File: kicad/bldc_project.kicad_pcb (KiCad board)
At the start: 4 copper layers, 158 parts, among them J1 Screw_Terminal_01x03, J2 Screw_Terminal_01x03, J3 Conn_ARM_SWD_TagConnect_TC203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, J4 TYPE-C-31-M-12, Q1 IRFZ44N, Q2 IRFZ44N, Q3 IRFZ44N, Q4 IRFZ44N, Q5 IRFZ44N, Q6 IRFZ44N, Q7 BC847BW,115, SW1 SW_Push, U1 ir2104, U10 MC34063AD, U11 MC34063AD, U12 LD1117S33TR_SOT223, U14 ir2104, U2 ir2104, U4 INA180A2, U5 INA180A2, U6 INA180A2, U7 STM32F303CBTx, Y1 8 MHz

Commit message: [kicad] basic placement of everything but power and inverter, changed the ldo, changed caps
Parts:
- removed U12: LD1117S33TR_SOT223, Package_TO_SOT_SMD:SOT-223-3_TabPin2
- added C47: 1uF, Capacitor_SMD:C_1206_3216Metric, F.Cu at (52.2, 107.3)
- added FB1: 120R, Resistor_SMD:R_0603_1608Metric, F.Cu at (48.7, 119.6)
- added U3: ir2104, Package_SO:SOIC-8-1EP_3.9x4.9mm_P1.27mm_EP2.29x3mm, F.Cu at (216.0, 112.6)
- C31: value 20pF -> 1uF; footprint Capacitor_SMD:C_0603_1608Metric -> Capacitor_SMD:C_1206_3216Metric
- C32: value 20pF -> 0.1uF; footprint Capacitor_SMD:C_0603_1608Metric -> Resistor_SMD:R_0402_1005Metric
- C35: value 0.1uF -> 20pF; footprint Resistor_SMD:R_0402_1005Metric -> Capacitor_SMD:C_0603_1608Metric
- C36: value 100uF -> 20pF; footprint Capacitor_SMD:C_1210_3225Metric -> Capacitor_SMD:C_0603_1608Metric
- C37: value 1uF -> 100uF; footprint Capacitor_SMD:C_1206_3216Metric -> Capacitor_SMD:C_1210_3225Metric
- C38: value 100uF -> 1uF; footprint Capacitor_SMD:C_1210_3225Metric -> Capacitor_SMD:C_1206_3216Metric
- C41: value 470pF -> 100uF; footprint Capacitor_SMD:C_0805_2012Metric -> Capacitor_SMD:C_1210_3225Metric
- C42: value 820pF -> 470pF
- C43: value 100uF -> 820pF; footprint Capacitor_SMD:C_1210_3225Metric -> Capacitor_SMD:C_0805_2012Metric
- C45: value 0.1uF -> 100uF; footprint Resistor_SMD:R_0402_1005Metric -> Capacitor_SMD:C_1210_3225Metric
- C46: value 10uF -> 1uF; footprint Capacitor_SMD:C_0402_1005Metric -> Capacitor_SMD:C_1206_3216Metric
- J1: value Screw_Terminal_01x03 -> Conn_ARM_SWD_TagConnect_TC2030-NL; footprint TerminalBlock:TerminalBlock_bornier-3_P5.08mm -> Connector:Tag-Connect_TC2030-IDC-NL_2x03_P1.27mm_Vertical
- J3: value Conn_ARM_SWD_TagConnect_TC2030-NL -> Screw_Terminal_01x03; footprint Connector:Tag-Connect_TC2030-IDC-NL_2x03_P1.27mm_Vertical -> TerminalBlock:TerminalBlock_bornier-3_P5.08mm
- R39, R40: value 4.7k -> 10; footprint Resistor_SMD:R_0805_2012Metric -> Resistor_SMD:R_1206_3216Metric
- R41: value 0 -> 10; footprint Resistor_SMD:R_0402_1005Metric -> Resistor_SMD:R_1206_3216Metric
- R44, R46: value 10 -> 4.7k; footprint Resistor_SMD:R_1206_3216Metric -> Resistor_SMD:R_0805_2012Metric
- R45: value 10 -> 0; footprint Resistor_SMD:R_1206_3216Metric -> Resistor_SMD:R_0402_1005Metric
- R49: value 1.5k -> 33k; footprint Resistor_SMD:R_0805_2012Metric -> Resistor_SMD:R_0603_1608Metric
- R51: value 33k -> 1.5k; footprint Resistor_SMD:R_0603_1608Metric -> Resistor_SMD:R_0805_2012Metric
- U14: value ir2104 -> XC6206P332MR-G; footprint Package_SO:SOIC-8-1EP_3.9x4.9mm_P1.27mm_EP2.29x3mm -> Package_TO_SOT_SMD:SOT-23
- moved R41 175.2 mm to (15.6, 148.0)
- moved R40 172.9 mm to (15.6, 155.2)
- moved R39 172.9 mm to (15.5, 151.8)
- moved C32 156.8 mm to (16.5, 143.9), turned to 90 degrees
- moved J3 156.6 mm to (48.5, 157.0), turned to 180 degrees
- moved J1 148.9 mm to (29.6, 151.2), turned to -90 degrees
- moved SW1 148.8 mm to (49.3, 146.1), turned to 90 degrees
- moved D4 148.1 mm to (20.1, 141.4), turned to 90 degrees
- moved R44 145.9 mm to (38.6, 148.1)
- moved C26 145.8 mm to (35.7, 125.4), turned to 90 degrees
- moved D5 142.4 mm to (24.6, 141.4), turned to 90 degrees
- moved C24 141.8 mm to (38.5, 116.8)
- moved U7 140.9 mm to (41.4, 122.5), turned to 180 degrees
- moved C23 140.8 mm to (44.2, 128.2), turned to 180 degrees
- moved R46 139.7 mm to (42.9, 148.0), turned to 180 degrees
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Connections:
- C29 pad 1: +3.3V -> +3.3VA
- C30 pad 1: +3.3V -> +3.3VA
- C31 pad 1: GND -> +3.3V
- C31 pad 2: Net-(C31-Pad2) -> GND
- C32 pad 1: GND -> /CPU/SWD_NRESET
- C32 pad 2: /CPU/HSE_IN -> GND
- C34 pad 1: Net-(J2-Pin_3) -> Net-(J2-Pin_2)
- C35 pad 1: /CPU/SWD_NRESET -> GND
- C35 pad 2: GND -> Net-(C35-Pad2)
- C36 pad 2: /POWER/VBUCK5_OUT -> /CPU/HSE_IN
- C37 pad 1: USB_VBUS -> GND
- C37 pad 2: GND -> /POWER/VBUCK5_OUT
- C38 pad 1: GND -> USB_VBUS
- C38 pad 2: +10V -> GND
- C39 pad 1: /POWER/VBUCK5_OUT -> GND
- C39 pad 2: GND -> +10V
- C4 pad 2: Net-(U14-VS) -> Net-(U1-VS)
- C40 pad 1: +10V -> /POWER/VBUCK5_OUT
- C41 pad 1: GND -> +10V
- C41 pad 2: Net-(U10-TC) -> GND
- C42 pad 2: Net-(U11-TC) -> Net-(U10-TC)
- C43 pad 1: +BATT -> GND
- C43 pad 2: GND -> Net-(U11-TC)
- C45 pad 1: +5V -> +BATT
- C46 pad 1: +3.3V -> +5V
- C5 pad 2: Net-(U1-VS) -> Net-(U2-VS)
- C6 pad 2: Net-(U2-VS) -> Net-(U3-VS)
- J1 pad 1: /CPU/I2C_SDA -> +3.3V
- J1 pad 2: /CPU/I2C_SCL -> Net-(D6-A1)
- J1 pad 3: GND -> Net-(D4-A1)
- J2 pad 1: Net-(J2-Pin_1) -> GND
- J2 pad 2: GND -> Net-(J2-Pin_2)
- J3 pad 1: +3.3V -> GND
- J3 pad 2: Net-(D6-A1) -> /CPU/I2C_SDA
- J3 pad 3: Net-(D4-A1) -> /CPU/I2C_SCL
- P1 pad 1: +BATT -> /DRIVER/PhaseU
- P2 pad 1: GND -> /DRIVER/PhaseV
- P3 pad 1: /DRIVER/PhaseU -> /DRIVER/PhaseW
- P4 pad 1: /DRIVER/PhaseV -> +BATT
- P5 pad 1: /DRIVER/PhaseW -> GND
- R39 pad 1: +3.3V -> /CPU/SWD_SWDIO
- R39 pad 2: /CPU/I2C_SDA -> Net-(D6-A1)
- R4 pad 1: Net-(U14-HO) -> Net-(U1-HO)
- R40 pad 1: +3.3V -> /CPU/SWD_SWCLK
- R40 pad 2: /CPU/I2C_SCL -> Net-(D5-A1)
- R41 pad 1: /CPU/HSE_OUT -> /CPU/SWD_NRESET
- R41 pad 2: Net-(C31-Pad2) -> Net-(D4-A1)
- R42 pad 1: Net-(J2-Pin_3) -> Net-(J2-Pin_2)
- R42 pad 2: Net-(J2-Pin_1) -> Net-(J2-Pin_3)
- R43 pad 1: Net-(J2-Pin_3) -> Net-(J2-Pin_2)
- R43 pad 2: Net-(J2-Pin_3) -> Net-(J2-Pin_2)
- R44 pad 1: /CPU/SWD_SWDIO -> +3.3V
- R44 pad 2: Net-(D6-A1) -> /CPU/I2C_SCL
- R45 pad 1: /CPU/SWD_SWCLK -> /CPU/HSE_OUT
- R45 pad 2: Net-(D5-A1) -> Net-(C35-Pad2)
- R46 pad 1: /CPU/SWD_NRESET -> +3.3V
- R46 pad 2: Net-(D4-A1) -> /CPU/I2C_SDA
- R49 pad 1: USB_RENUMn -> USB_VBUS
- R49 pad 2: Net-(Q7-B) -> USB_SENSE
- R5 pad 1: Net-(U14-LO) -> Net-(U1-LO)
- R50 pad 1: USB_VBUS -> USB_SENSE
- R50 pad 2: USB_SENSE -> GND
- R51 pad 1: USB_SENSE -> USB_RENUMn
- R51 pad 2: GND -> Net-(Q7-B)
- R6 pad 1: Net-(U2-HO) -> Net-(U3-HO)
- R7 pad 1: Net-(U2-LO) -> Net-(U3-LO)
- R8 pad 1: Net-(U1-HO) -> Net-(U2-HO)
- R9 pad 1: Net-(U1-LO) -> Net-(U2-LO)
- U1 pad 2: PhaseV_SWITCH -> PhaseU_SWITCH
- U1 pad 3: PhaseV_SD -> PhaseU_SD
- U1 pad 8: Net-(D2-K) -> Net-(D1-K)
- U14 pad 1: +10V -> GND
- U14 pad 2: PhaseU_SWITCH -> +3.3V
- U14 pad 3: PhaseU_SD -> +5V
- U2 pad 2: PhaseW_SWITCH -> PhaseV_SWITCH
- U2 pad 3: PhaseW_SD -> PhaseV_SD
- U2 pad 8: Net-(D3-K) -> Net-(D2-K)
- U7 pad 9: +3.3V -> +3.3VA
- U8 pad 6: Net-(J2-Pin_3) -> Net-(J2-Pin_2)
- U8 pad 7: Net-(J2-Pin_1) -> Net-(J2-Pin_3)
- Y1 pad 3: Net-(C31-Pad2) -> Net-(C35-Pad2)

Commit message: [kicad] positioning of single inverter stage
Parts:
- moved H5 233.8 mm to (22.4, 18.6), turned to 90 degrees
- moved H6 227.1 mm to (29.5, 18.6), turned to 90 degrees
- moved H3 226.5 mm to (22.4, 25.6), turned to 90 degrees
- moved H4 219.7 mm to (29.5, 25.6), turned to 90 degrees
- moved H1 219.5 mm to (22.4, 32.6), turned to 90 degrees
- moved H2 212.4 mm to (29.5, 32.6), turned to 90 degrees
- moved C21 82.2 mm to (147.5, 124.1)
- moved R19 81.2 mm to (253.2, 63.0)
- moved R13 81.2 mm to (249.2, 63.0)
- moved R31 79.8 mm to (206.0, 58.8)
- moved R29 79.8 mm to (206.0, 53.8)
- moved R30 79.8 mm to (206.0, 56.3)
- moved C1 78.3 mm to (233.5, 63.0)
- moved C10 78.3 mm to (224.1, 63.6)
- moved C13 78.3 mm to (226.9, 63.6)
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
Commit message: [kicad] Removed ESD diodes for SWD, changed SWD resistor to smaller size
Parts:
- removed D4, D5, D6: SMAJ6.5CA, Diode_SMD:D_SMA
- R39, R40, R41: footprint Resistor_SMD:R_1206_3216Metric -> Resistor_SMD:R_0402_1005Metric
- moved U1 130.5 mm to (124.3, 84.5)
- moved U2 128.3 mm to (124.2, 112.9)
- moved R25 125.3 mm to (144.8, 109.8), turned to -90 degrees
- moved R1 124.5 mm to (122.8, 80.2)
- moved C4 120.6 mm to (131.0, 83.7), turned to -90 degrees
- moved R2 120.2 mm to (122.9, 108.8)
- moved R28 119.8 mm to (151.4, 92.6), turned to 90 degrees
- moved C5 119.5 mm to (129.8, 112.0), turned to -90 degrees
- moved P1 118.9 mm to (164.1, 98.5)
- moved C1 116.2 mm to (118.8, 81.6), turned to 90 degrees
- moved P2 114.4 mm to (164.1, 114.6)
- moved R20 113.5 mm to (139.5, 107.9), turned to 90 degrees
- moved C2 113.4 mm to (118.6, 109.8), turned to 90 degrees
- moved R19 112.5 mm to (142.0, 80.5), turned to -90 degrees
- moved R5 112.5 mm to (133.5, 86.4)
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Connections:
- C34 pad 1: Net-(J2-Pin_2) -> /CPU/CAN_N
- J2 pad 2: Net-(J2-Pin_2) -> /CPU/CAN_H
- J2 pad 3: Net-(J2-Pin_3) -> /CPU/CAN_L
- R42 pad 1: Net-(J2-Pin_2) -> /CPU/CAN_N
- R42 pad 2: Net-(J2-Pin_3) -> /CPU/CAN_H
- R43 pad 1: Net-(J2-Pin_2) -> /CPU/CAN_L
- R43 pad 2: Net-(J2-Pin_2) -> /CPU/CAN_N
- U8 pad 6: Net-(J2-Pin_2) -> /CPU/CAN_L
- U8 pad 7: Net-(J2-Pin_3) -> /CPU/CAN_H

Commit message: started routing
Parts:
- moved C38 10.4 mm to (75.3, 108.2)
- moved R61 10.4 mm to (76.5, 103.4)
- moved R62 10.4 mm to (75.0, 104.9)
- moved R63 10.4 mm to (79.4, 108.2)
- moved U13 10.4 mm to (78.0, 105.5)
- moved D9 9.14 mm to (82.3, 109.0)
- moved C46 7.38 mm to (78.7, 111.2)
- moved C47 7.11 mm to (70.8, 111.1), turned to 90 degrees
- moved U14 6.19 mm to (74.4, 111.6), turned to 0 degrees
- moved SW1 3.27 mm to (51.0, 120.3), turned to 180 degrees
- moved C33 2.92 mm to (54.6, 123.6)
- moved U8 2.55 mm to (54.2, 126.5)
- moved C34 2.55 mm to (54.1, 130.8)
- moved R42 2.55 mm to (56.1, 130.8)
- moved R43 2.55 mm to (52.1, 130.8)
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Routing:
- net +3.3V: track 0.00 -> 8.05 mm
- net /CPU/HSE_OUT: track 0.00 -> 6.01 mm
- net +3.3VA: track 0.00 -> 5.03 mm
- net /CPU/HSE_IN: track 0.00 -> 5.01 mm
- net GND: track 0.00 -> 4.94 mm
- net Net-(C35-Pad2): track 0.00 -> 4.36 mm

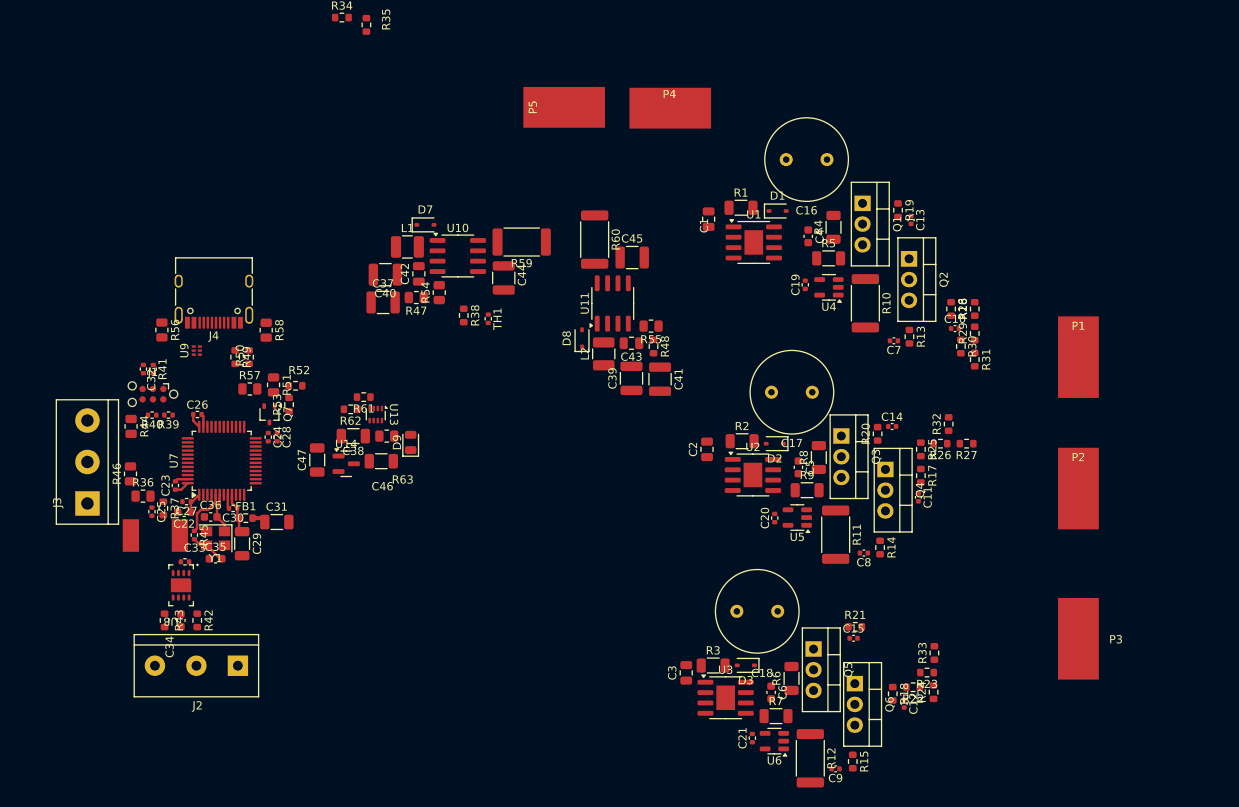
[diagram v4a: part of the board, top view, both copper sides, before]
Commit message: [kicad] Experimented with component placing
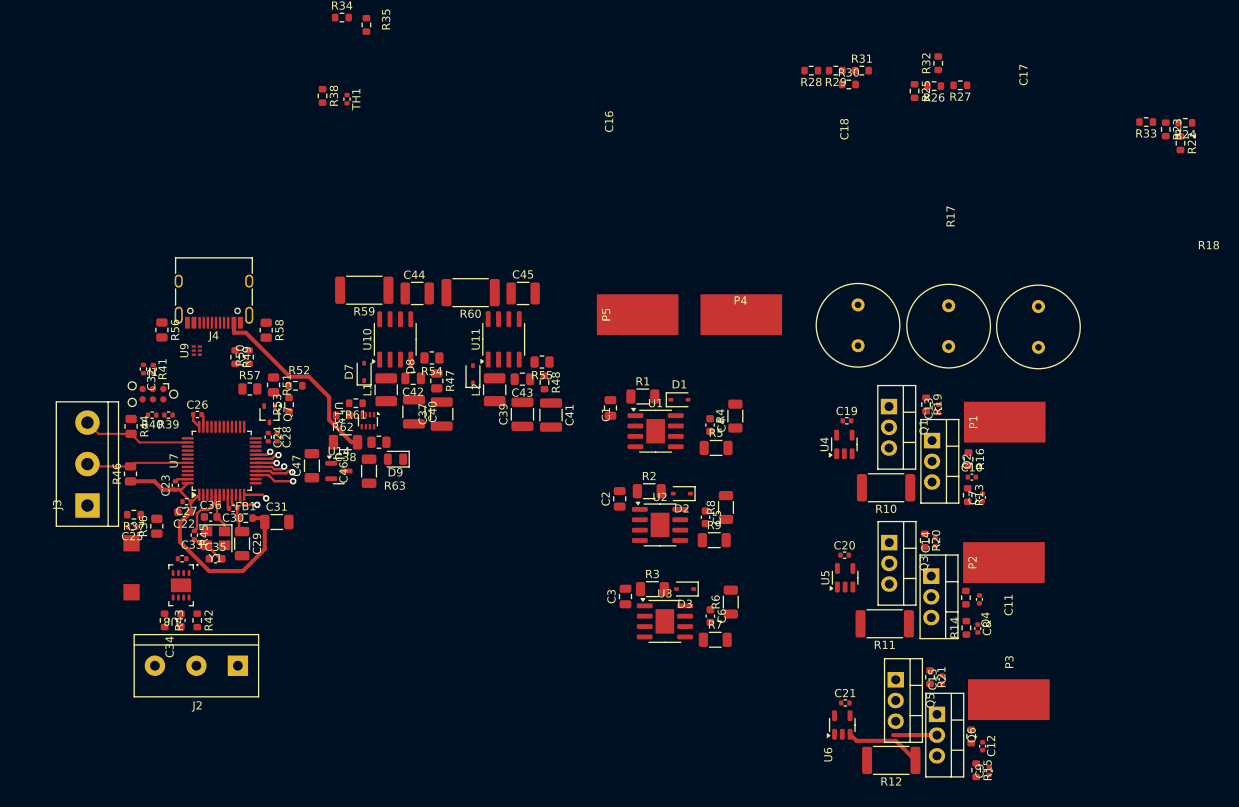
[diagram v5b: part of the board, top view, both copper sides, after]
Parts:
- moved R24 76.3 mm to (177.2, 69.8), turned to 180 degrees
- moved R22 74.3 mm to (176.6, 72.3), turned to -90 degrees
- moved R23 72.7 mm to (174.8, 70.6), turned to -90 degrees
- moved R33 70.0 mm to (172.4, 69.7), turned to 180 degrees
- moved R32 44.2 mm to (146.9, 62.5)
- moved R25 43.9 mm to (144.0, 65.9)
- moved R27 43.9 mm to (149.6, 65.2)
- moved R26 43.8 mm to (146.4, 65.3)
- moved C18 38.6 mm to (148.2, 97.2), turned to 90 degrees
- moved R31 38.0 mm to (137.6, 63.4), turned to 0 degrees
- moved R29 36.4 mm to (134.4, 63.4), turned to 180 degrees
- moved R28 35.4 mm to (131.4, 63.4), turned to 180 degrees
- moved R30 34.9 mm to (136.0, 65.1), turned to 0 degrees
- moved R38 32.0 mm to (71.5, 66.5)
- moved TH1 32.0 mm to (74.5, 66.9)
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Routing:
- net +3.3V: track 8.05 -> 36.9 mm
- net USB_VBUS: track 0.00 -> 23.6 mm
- net /CPU/I2C_SCL: track 0.00 -> 13.3 mm
- net /CPU/I2C_SDA: track 0.00 -> 12.6 mm
- net /DRIVER/PhaseW_CURRENT+: track 0.00 -> 9.34 mm
- net Net-(Q6-G): track 0.00 -> 5.39 mm
- net PhaseU_DIV: track 0.00 -> 4.90 mm, vias 0 -> 1
- net PhaseV_DIV: track 0.00 -> 4.80 mm, vias 0 -> 1
- net PhaseV_SWITCH: track 0.00 -> 3.74 mm, vias 0 -> 1
- net /CPU/MEAS_TEMP: track 0.00 -> 3.11 mm, vias 0 -> 1
- net PhaseU_SD: track 0.00 -> 2.97 mm, vias 0 -> 1
- net /CPU/MEAS_BAT: track 0.00 -> 2.88 mm, vias 0 -> 1
- net PhaseU_SWITCH: track 0.00 -> 2.77 mm, vias 0 -> 1
- net PhaseW_DIV: track 0.00 -> 1.93 mm, vias 0 -> 1

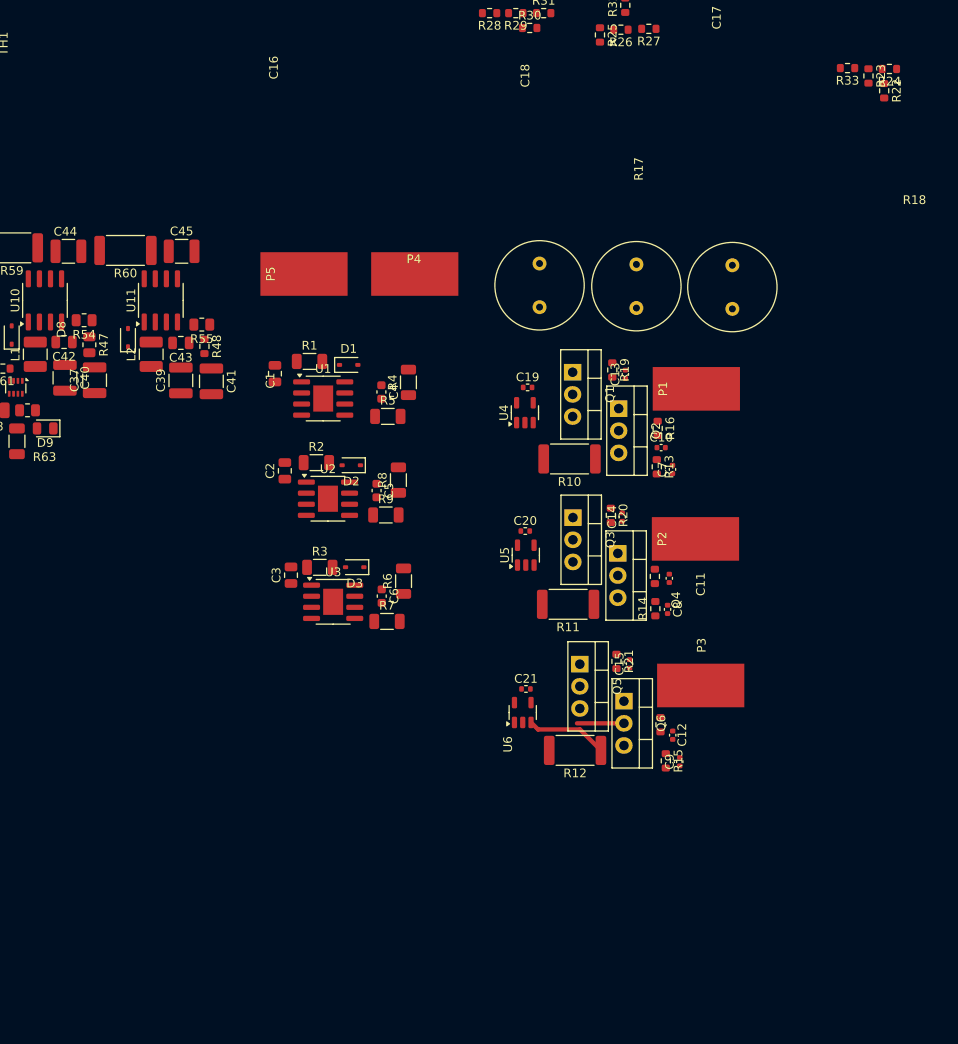
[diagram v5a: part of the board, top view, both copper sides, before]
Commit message: [bldc] did minor position changing
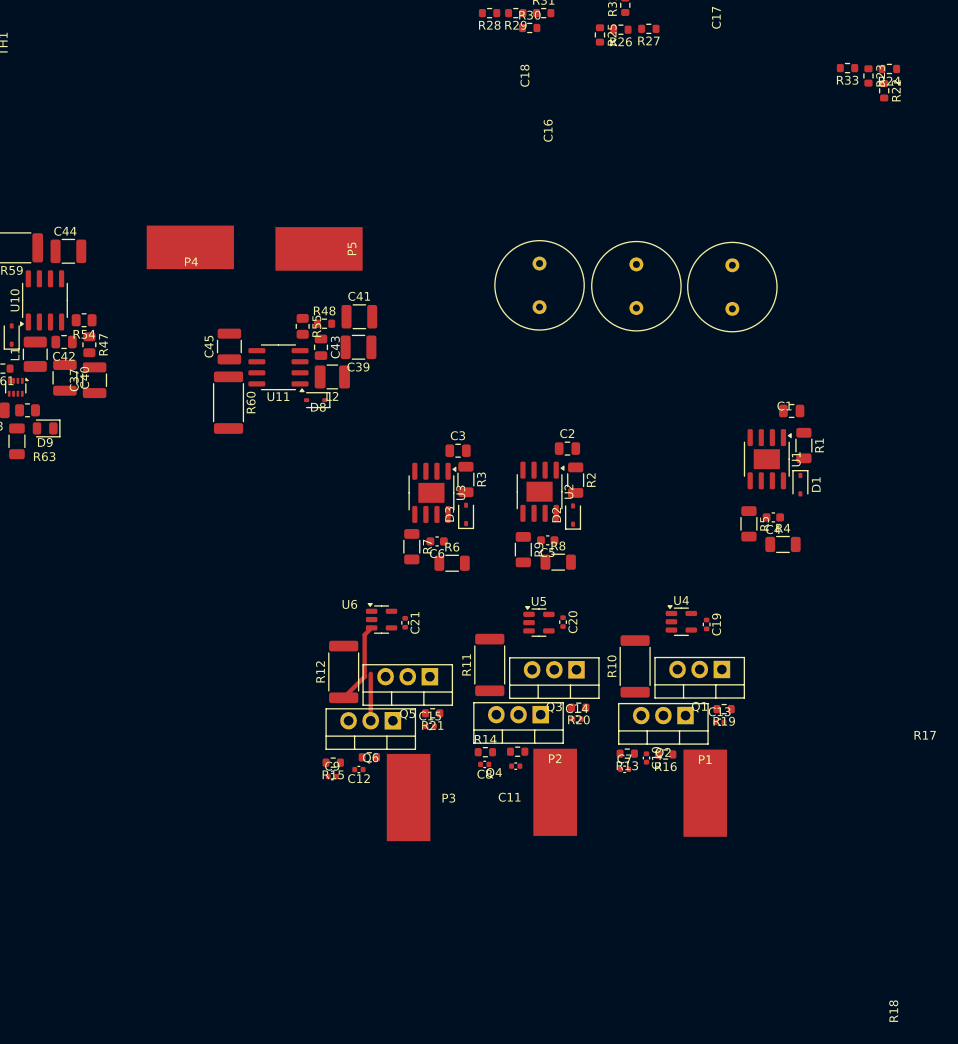
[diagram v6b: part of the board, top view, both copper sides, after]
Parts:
- moved C1 59.4 mm to (166.0, 109.0), turned to 0 degrees
- moved R1 57.5 mm to (167.4, 113.0), turned to -90 degrees
- moved D1 53.6 mm to (167.0, 117.5), turned to -90 degrees
- moved U1 51.3 mm to (163.2, 114.5), turned to -90 degrees
- moved C4 47.2 mm to (163.9, 121.2), turned to 180 degrees
- moved R4 46.8 mm to (165.0, 124.3), turned to 0 degrees
- moved P1 46.4 mm to (156.1, 152.8), turned to 0 degrees
- moved R5 43.2 mm to (161.1, 121.9), turned to -90 degrees
- moved C13 41.3 mm to (157.8, 144.7), turned to 0 degrees
- moved R19 40.9 mm to (158.3, 143.2), turned to 180 degrees
- moved C9 39.9 mm to (113.4, 150.9), turned to 0 degrees
- moved Q1 38.1 mm to (158.0, 138.6), turned to 180 degrees
- moved R15 38.1 mm to (113.5, 149.3), turned to 180 degrees
- moved R16 37.4 mm to (151.6, 148.4), turned to 180 degrees
- moved C12 36.2 mm to (116.4, 150.1), turned to 180 degrees
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
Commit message: [kicad] Changed mounting hole to jlcpcb type, poured 2 gnd layers, started with traces.
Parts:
- removed the H3 at (22.4, 25.6)
- removed H5: MountingHole, MountingHole:MountingHole_3.2mm_M3_ISO14580
- H1, H2, H4: footprint MountingHole:MountingHole_3.2mm_M3_ISO14580 -> bldc:MountingHole_1.152mm_jlcpcb
- H3: renamed from H6; footprint MountingHole:MountingHole_3.2mm_M3_ISO14580 -> bldc:MountingHole_1.152mm_jlcpcb
- moved H2 158.3 mm to (149.1, 136.4)
- moved H1 136.9 mm to (149.1, 84.6)
- moved R24 117.9 mm to (77.8, 133.2), turned to 90 degrees
- moved R33 117.0 mm to (73.1, 131.5), turned to 90 degrees
- moved R22 116.3 mm to (79.5, 136.3)
- moved R23 114.1 mm to (79.4, 133.2)
- moved H4 111.5 mm to (42.3, 136.4)
- moved R32 102.5 mm to (71.2, 131.6)
- moved R31 96.4 mm to (69.5, 131.6), turned to 90 degrees
- moved R27 87.3 mm to (94.8, 133.2), turned to 90 degrees
- moved R25 85.0 mm to (96.6, 136.4)
- moved R26 84.2 mm to (96.6, 133.2), turned to -90 degrees
- moved R28 74.1 mm to (115.2, 135.7), turned to -90 degrees
- moved R29 71.8 mm to (115.2, 132.5), turned to -90 degrees
- moved R30 71.1 mm to (113.4, 132.5), turned to 90 degrees
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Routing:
- net USB_VBUS: track 23.6 -> 0.00 mm
- net /CPU/I2C_SDA: track 12.6 -> 0.00 mm
- net +3.3V: track 36.9 -> 48.0 mm
- net +10V: track 0.00 -> 10.7 mm
- net /DRIVER/PhaseW_CURRENT+: track 9.34 -> 0.00 mm
- net Net-(U11-Vfb): track 0.00 -> 8.20 mm
- net Net-(R36-Pad1): track 0.00 -> 7.12 mm
- net /CPU/I2C_SCL: track 13.3 -> 7.37 mm
- net Net-(D8-K): track 0.00 -> 5.62 mm
- net /DRIVER/PhaseV: track 0.00 -> 5.55 mm
- net Net-(Q6-G): track 5.39 -> 0.00 mm
- net /CPU/CAN_TX: track 0.00 -> 3.74 mm, vias 0 -> 1
- net /CPU/CAN_RX: track 0.00 -> 3.56 mm, vias 0 -> 3
- net Net-(U3-VS): track 0.00 -> 3.31 mm
- net Net-(D3-K): track 0.00 -> 3.29 mm
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- added copper zone on In1.Cu, net GND
- added copper zone on In2.Cu, net GND
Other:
- board outline added: 115 x 60 mm
- board text added: "# INVERTER POSITIONING - Keep the actual inverter as close as possible to the Vbat - Therefor keep the inverter to the left side - Keep the capacitors and 10 V converter to the left # POWER SIGNALS - 10 V signals - The 3.3 V routing will need to go through the 3rd layer underneath the VBATT+ (OPAMP) - The 5 V routing will need to go underneath the 3.3 V power or vice versa to deliver power to the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"
